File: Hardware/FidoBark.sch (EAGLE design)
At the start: 65 parts, among them Q1 MMBT2222A, T1 BPX81, U1 EDISON_CONNECTOR_FULLHEADER, U2 FTS31XS-U, U3 MCP73831, U4 TXB0108, U5 ADS1015, U6 PCA9306, U8 LSM9DS0

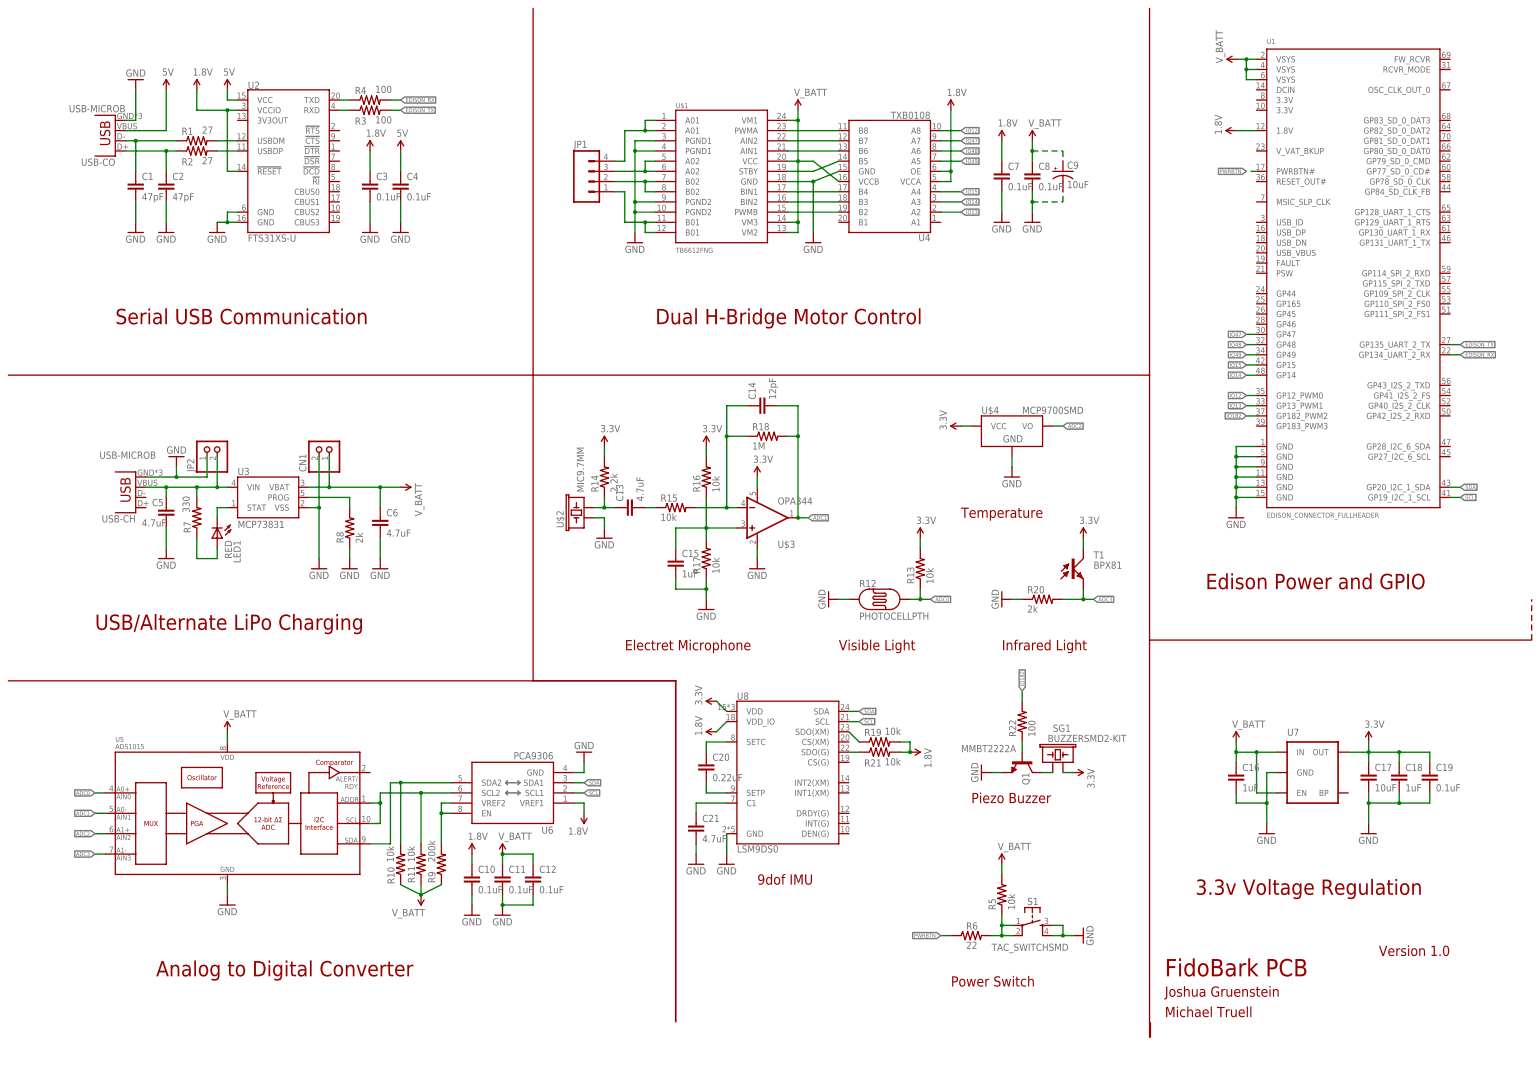
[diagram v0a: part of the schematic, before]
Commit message: simplification
removed any hardware serial communication: it will need to be connected
to wifi in order to debug/upload code
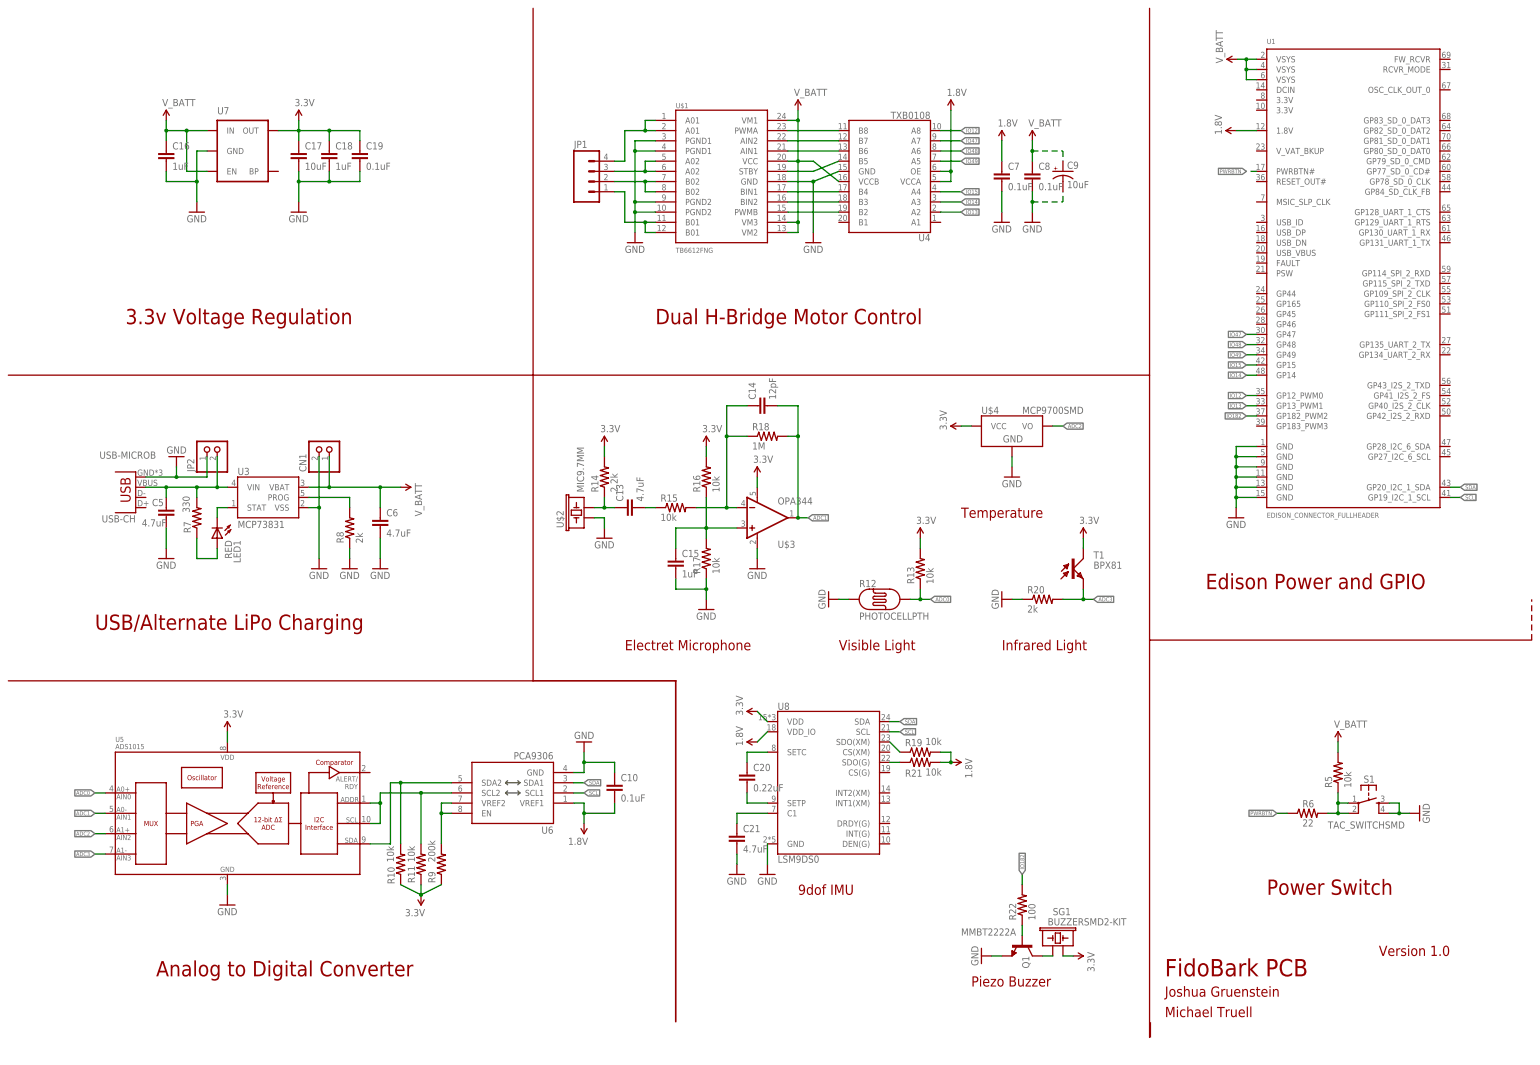
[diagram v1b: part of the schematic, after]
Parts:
- removed C1, C2: 47pF, SparkFun-Passives:CAP0603-CAP
- removed C11, C12, C3, C4: 0.1uF, SparkFun-Passives:CAP0603-CAP
- removed R1, R2: 27, adafruit:R-US_R0603
- removed R3, R4: 100, adafruit:R-US_R0603
- removed U2: FTS31XS-U, SparkFun-DigitalIC:FT231XS
- removed USB-CO: USB-MICROB, SparkFun-Connectors:USB-MICROB
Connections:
- removed net 5V: C4.1, U2.VCC, USB-CO.VBUS
- removed net EDISON_RX: R4.2, U1.GP134_UART_2_RX
- removed net EDISON_TX: R3.2, U1.GP135_UART_2_TX
- removed net N$1: R2.2, U2.USBDP
- removed net N$2: R1.2, U2.USBDM
- removed net N$3: R3.1, U2.RXD
- removed net N$4: C2.1, R2.1, USB-CO.D+
- removed net N$5: C1.1, R1.1, USB-CO.D-
- removed net N$6: R4.1, U2.TXD
- net 1.8V: now also C10.2; no longer C10.1, C3.1, U2.!RESET, U2.VCCIO
- net 3.3V: now also R10.1, R11.1, R9.1, U5.VDD
- net GND: now also C10.1; no longer C1.2, C10.2, C11.2, C12.2, C2.2, C3.2, C4.2, U2.GND@16, U2.GND@6, USB-CO.GND
- net V_BATT: no longer C11.1, C12.1, R10.1, R11.1, R9.1, U5.VDD
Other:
- note removed: "Serial USB Communication"
- moved on the sheet: C10, C16, C17, C18, C19, C20, C21, Q1, R19, R21, R22, R5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

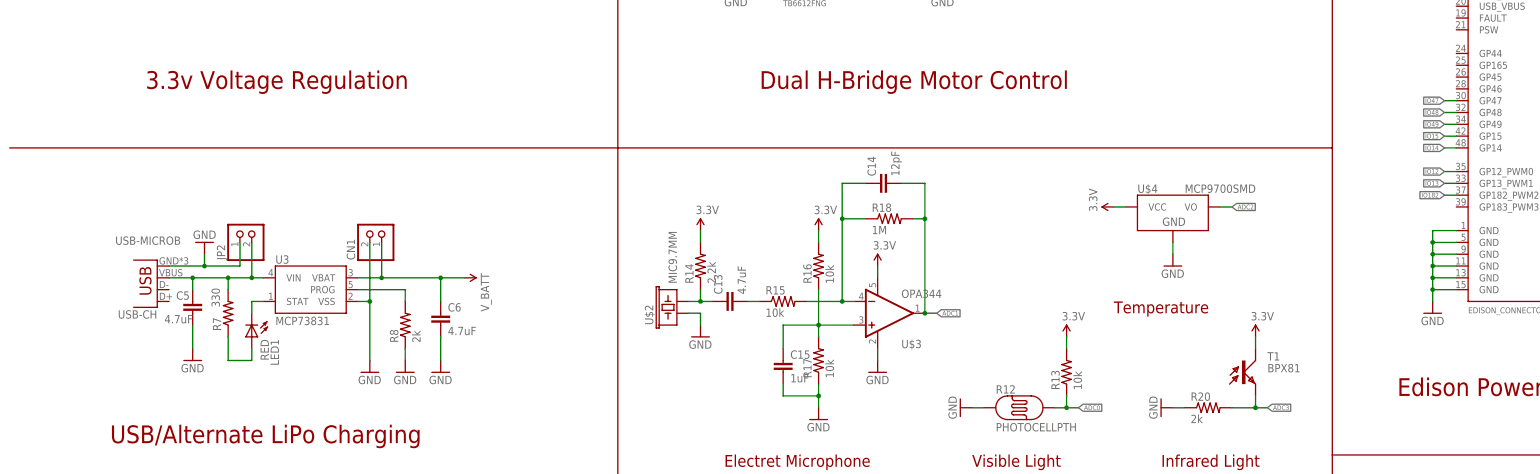
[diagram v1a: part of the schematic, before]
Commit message: battery level and charge sensing
eliminated the temperature sensor, as it took up an ADC port and is
hard to use as a training device
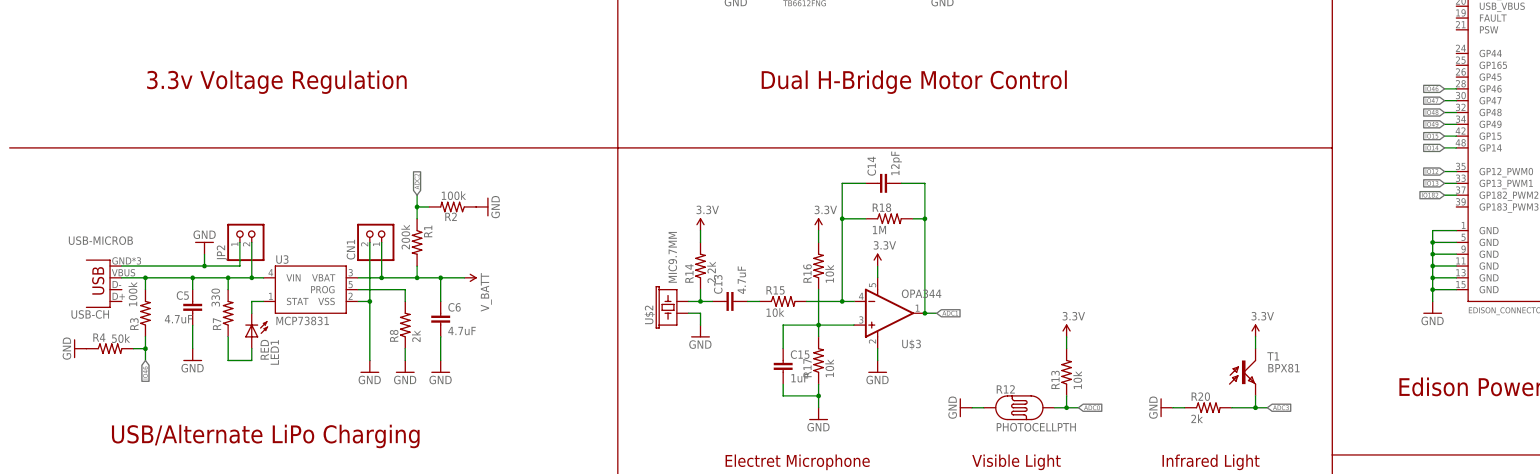
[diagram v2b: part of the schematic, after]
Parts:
- removed U$4: MCP9700SMD, SparkFun-Sensors:MCP9700SMD
- added R1: 200k, adafruit:R-US_R0603
- added R2, R3: 100k, adafruit:R-US_R0603
- added R4: 50k, adafruit:R-US_R0603
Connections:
- new net IO46: R3.1, R4.2, U1.GP46
- net 3.3V: no longer U$4.VCC
- net ADC2: now also R1.1, R2.2; no longer U$4.VO
- net GND: now also R2.1, R4.1; no longer U$4.GND
- net N$12: now also R3.2
- net V_BATT: now also R1.2
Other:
- note removed: "Temperature"
- moved on the sheet: USB-CH
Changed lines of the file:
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@@
 <part name="C15" library="SparkFun-Passives" deviceset="CAP" device="0603-CAP" value="1uF"/>
 <part name="U$3" library="SparkFun-AnalogIC" deviceset="OPA344" device=""/>
-<part name="U$4" library="SparkFun-Sensors" deviceset="MCP9700" device="SMD"/>
-<part name="SUPPLY24" library="SparkFun-Aesthetics" deviceset="3.3V" device=""/>
-<part name="GND23" library="supply1" deviceset="GND" device=""/>
 <part name="T1" library="opto-trans-siemens" deviceset="BPX81" device=""/>
 <part name="GND24" library="supply1" deviceset="GND" device=""/>
@@
 <part name="SUPPLY1" library="SparkFun-Aesthetics" deviceset="3.3V" device=""/>
 <part name="SUPPLY2" library="SparkFun-Aesthetics" deviceset="3.3V" device=""/>
+<part name="R1" library="adafruit" deviceset="R-US_" device="R0603" value="200k"/>
+<part name="R2" library="adafruit" deviceset="R-US_" device="R0603" value="100k"/>
+<part name="GND1" library="supply1" deviceset="GND" device=""/>
+<part name="R3" library="adafruit" deviceset="R-US_" device="R0603" value="100k"/>
+<part name="R4" library="adafruit" deviceset="R-US_" device="R0603" value="50k"/>
+<part name="GND2" library="supply1" deviceset="GND" device=""/>
 </parts>
 <sheets>
@@
 <text x="157.48" y="96.52" size="2.54" layer="94" font="vector">Electret Microphone</text>
 <text x="210.82" y="96.52" size="2.54" layer="94" font="vector">Visible Light</text>
-<text x="241.3" y="129.54" size="2.54" layer="94" font="vector">Temperature</text>
 <text x="251.46" y="96.52" size="2.54" layer="94" font="vector">Infrared Light</text>
 <text x="200.66" y="35.56" size="2.54" layer="94" font="vector">9dof IMU</text>
@@
 <attribute name="VALUE" x="57.785" y="123.952" size="1.778" layer="96" rot="R270"/>
 </instance>
-<instance part="USB-CH" gate="G$1" x="35.56" y="139.7" smashed="yes" rot="R180">
-<attribute name="NAME" x="35.56" y="130.175" size="1.778" layer="95" rot="R180"/>
-<attribute name="VALUE" x="40.64" y="146.05" size="1.778" layer="96" rot="R180"/>
+<instance part="USB-CH" gate="G$1" x="25.4" y="139.7" smashed="yes" rot="R180">
+<attribute name="NAME" x="25.4" y="130.175" size="1.778" layer="95" rot="R180"/>
+<attribute name="VALUE" x="30.48" y="146.05" size="1.778" layer="96" rot="R180"/>
 </instance>
 <instance part="SUPPLY6" gate="G$1" x="101.6" y="137.16" rot="R270"/>
@@
 <instance part="C15" gate="G$1" x="170.18" y="116.84"/>
 <instance part="U$3" gate="G$1" x="190.5" y="129.54"/>
-<instance part="U$4" gate="G$1" x="254" y="149.86"/>
-<instance part="SUPPLY24" gate="G$1" x="241.3" y="152.4" rot="R90"/>
-<instance part="GND23" gate="1" x="254" y="139.7"/>
 <instance part="T1" gate="1" x="269.24" y="116.84"/>
 <instance part="GND24" gate="1" x="251.46" y="109.22" rot="R270"/>
@@
 <instance part="SUPPLY1" gate="G$1" x="58.42" y="76.2"/>
 <instance part="SUPPLY2" gate="G$1" x="106.68" y="35.56" rot="R180"/>
+<instance part="R1" gate="G$1" x="91.44" y="144.78" smashed="yes" rot="R270">
+<attribute name="NAME" x="92.9386" y="148.59" size="1.778" layer="95" rot="R270"/>
+<attribute name="VALUE" x="88.138" y="148.59" size="1.778" layer="96" rot="R270"/>
+</instance>
+<instance part="R2" gate="G$1" x="99.06" y="152.4" smashed="yes" rot="R180">
+<attribute name="NAME" x="97.282" y="149.3774" size="1.778" layer="95"/>
+<attribute name="VALUE" x="96.52" y="153.924" size="1.778" layer="96"/>
+</instance>
+<instance part="GND1" gate="1" x="106.68" y="152.4" rot="R90"/>
+<instance part="R3" gate="G$1" x="33.02" y="129.54" smashed="yes" rot="R90">
+<attribute name="NAME" x="31.5214" y="125.73" size="1.778" layer="95" rot="R90"/>
+<attribute name="VALUE" x="31.242" y="130.81" size="1.778" layer="96" rot="R90"/>
+</instance>
+<instance part="R4" gate="G$1" x="25.4" y="121.92" smashed="yes">
+<attribute name="NAME" x="21.59" y="123.4186" size="1.778" layer="95"/>
+<attribute name="VALUE" x="25.654" y="123.19" size="1.778" layer="96"/>
+</instance>
+<instance part="GND2" gate="1" x="17.78" y="121.92" rot="R270"/>
 </instances>
 <busses>
@@
 <pinref part="USB-CH" gate="G$1" pin="GND"/>
 <pinref part="GND10" gate="1" pin="GND"/>
-<wire x1="38.1" y1="139.7" x2="45.72" y2="139.7" width="0.1524" layer="91"/>
+<wire x1="27.94" y1="139.7" x2="45.72" y2="139.7" width="0.1524" layer="91"/>
 <wire x1="45.72" y1="139.7" x2="45.72" y2="142.24" width="0.1524" layer="91"/>
 <wire x1="45.72" y1="139.7" x2="53.34" y2="139.7" width="0.1524" layer="91"/>
@@
 </segment>
 <segment>
-<pinref part="U$4" gate="G$1" pin="GND"/>
-<pinref part="GND23" gate="1" pin="GND"/>
-<wire x1="254" y1="144.78" x2="254" y2="142.24" width="0.1524" layer="91"/>
-</segment>
-<segment>
 <pinref part="GND24" gate="1" pin="GND"/>
 <wire x1="254" y1="109.22" x2="256.54" y2="109.22" width="0.1524" layer="91"/>
@@
 <wire x1="248.92" y1="20.32" x2="251.46" y2="20.32" width="0.1524" layer="91"/>
 </segment>
+<segment>
+<pinref part="R2" gate="G$1" pin="1"/>
+<pinref part="GND1" gate="1" pin="GND"/>
+</segment>
+<segment>
+<pinref part="R4" gate="G$1" pin="1"/>
+<pinref part="GND2" gate="1" pin="GND"/>
+</segment>
 </net>
 <net name="N$7" class="0">
@@
 <segment>
 <pinref part="U3" gate="G$1" pin="VIN"/>
-<wire x1="38.1" y1="137.16" x2="43.18" y2="137.16" width="0.1524" layer="91"/>
 <pinref part="C5" gate="G$1" pin="1"/>
+<wire x1="27.94" y1="137.16" x2="33.02" y2="137.16" width="0.1524" layer="91"/>
+<wire x1="33.02" y1="137.16" x2="43.18" y2="137.16" width="0.1524" layer="91"/>
 <wire x1="43.18" y1="137.16" x2="50.8" y2="137.16" width="0.1524" layer="91"/>
 <wire x1="50.8" y1="137.16" x2="55.88" y2="137.16" width="0.1524" layer="91"/>
@@
 <wire x1="55.88" y1="144.78" x2="55.88" y2="137.16" width="0.1524" layer="91"/>
 <junction x="55.88" y="137.16"/>
+<pinref part="R3" gate="G$1" pin="2"/>
+<wire x1="33.02" y1="137.16" x2="33.02" y2="134.62" width="0.1524" layer="91"/>
+<junction x="33.02" y="137.16"/>
 </segment>
 </net>
 <net name="V_BATT" class="0">
 <segment>
-<pinref part="U3" gate="G$1" pin="VBAT"/>
 <pinref part="C6" gate="G$1" pin="1"/>
-<wire x1="78.74" y1="137.16" x2="83.82" y2="137.16" width="0.1524" layer="91"/>
-<wire x1="83.82" y1="137.16" x2="96.52" y2="137.16" width="0.1524" layer="91"/>
 <wire x1="96.52" y1="137.16" x2="96.52" y2="132.08" width="0.1524" layer="91"/>
 <wire x1="96.52" y1="137.16" x2="101.6" y2="137.16" width="0.1524" layer="91"/>
-<junction x="96.52" y="137.16"/>
 <pinref part="SUPPLY6" gate="G$1" pin="V_BATT"/>
 <pinref part="CN1" gate="G$1" pin="2"/>
 <wire x1="83.82" y1="144.78" x2="83.82" y2="137.16" width="0.1524" layer="91"/>
+<pinref part="U3" gate="G$1" pin="VBAT"/>
+<wire x1="78.74" y1="137.16" x2="83.82" y2="137.16" width="0.1524" layer="91"/>
+<wire x1="83.82" y1="137.16" x2="91.44" y2="137.16" width="0.1524" layer="91"/>
 <junction x="83.82" y="137.16"/>
+<junction x="96.52" y="137.16"/>
+<pinref part="R1" gate="G$1" pin="2"/>
+<wire x1="91.44" y1="137.16" x2="96.52" y2="137.16" width="0.1524" layer="91"/>
+<wire x1="91.44" y1="137.16" x2="91.44" y2="139.7" width="0.1524" layer="91"/>
+<junction x="91.44" y="137.16"/>
 </segment>
 <segment>
@@
 </segment>
 <segment>
-<pinref part="SUPPLY24" gate="G$1" pin="3.3V"/>
-<pinref part="U$4" gate="G$1" pin="VCC"/>
-<wire x1="241.3" y1="152.4" x2="243.84" y2="152.4" width="0.1524" layer="91"/>
-</segment>
-<segment>
 <pinref part="SUPPLY25" gate="G$1" pin="3.3V"/>
 <wire x1="271.78" y1="121.92" x2="271.78" y2="124.46" width="0.1524" layer="91"/>
@@
 </segment>
 <segment>
-<pinref part="U$4" gate="G$1" pin="VO"/>
-<wire x1="264.16" y1="152.4" x2="266.7" y2="152.4" width="0.1524" layer="91"/>
-<label x="266.7" y="152.4" size="1.016" layer="95" font="vector" xref="yes"/>
+<pinref part="R1" gate="G$1" pin="1"/>
+<wire x1="91.44" y1="149.86" x2="91.44" y2="152.4" width="0.1524" layer="91"/>
+<pinref part="R2" gate="G$1" pin="2"/>
+<wire x1="91.44" y1="152.4" x2="91.44" y2="154.94" width="0.1524" layer="91"/>
+<wire x1="91.44" y1="152.4" x2="93.98" y2="152.4" width="0.1524" layer="91"/>
+<junction x="91.44" y="152.4"/>
+<label x="91.44" y="154.94" size="1.016" layer="95" rot="R90" xref="yes"/>
 </segment>
 </net>
@@
 </segment>
 </net>
+<net name="IO46" class="0">
+<segment>
+<pinref part="U1" gate="G$1" pin="GP46"/>
+<wire x1="314.96" y1="177.8" x2="312.42" y2="177.8" width="0.1524" layer="91"/>
+<label x="312.42" y="177.8" size="1.016" layer="95" rot="R180" xref="yes"/>
+</segment>
+<segment>
+<pinref part="R3" gate="G$1" pin="1"/>
+<wire x1="33.02" y1="124.46" x2="33.02" y2="121.92" width="0.1524" layer="91"/>
+<wire x1="33.02" y1="121.92" x2="33.02" y2="119.38" width="0.1524" layer="91"/>
+<wire x1="33.02" y1="121.92" x2="30.48" y2="121.92" width="0.1524" layer="91"/>
+<junction x="33.02" y="121.92"/>
+<pinref part="R4" gate="G$1" pin="2"/>
+<label x="33.02" y="119.38" size="1.016" layer="95" rot="R270" xref="yes"/>
+</segment>
+</net>
